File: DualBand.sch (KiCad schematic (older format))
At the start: 23 parts, among them U1 LM7322QMAX/NOPB

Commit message: Connecting MCU
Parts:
- added C? (x2): 1u, symbol C
- added C? (x2): 0.01u, symbol C
- added R? (x2): R, symbol R
- added R?: 12k, symbol R
- added R?: 78.7k, symbol R
- added U?: LMH6703MA/NOPB, symbol LMH6703MA/NOPB
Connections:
- net labels added: DataIn
- wire segments 61 -> 96
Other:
- moved on the sheet: C?, D?, P?, R?, U1, U?

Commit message: Schematic almost finished. Needs headers and test points.
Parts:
- added C1, C10, C12, C2, C6, C8: 1u, symbol C
- added C11, C14, C3, C4, C5, C7, C9: 0.01u, symbol C
- added J1: Conn_01x02_Male, symbol Conn_01x02_Male
- added J2: Conn_01x16_Male, symbol Conn_01x16_Male
- added J3: Conn_01x01_Male, symbol Conn_01x01_Male
- added P1: CONN_01X03, symbol CONN_01X03
- added R3, R4: 10k, symbol R
- added SW1: SW_Push, symbol SW_Push
- R10, R13: renamed from R?; value R -> 100
- R11: renamed from R?; value 287 -> 75
- R14: renamed from R?; value R -> 220
- R7: renamed from R?; value R -> 3k
- R8: renamed from R?; value R -> 10
- R9: renamed from R?; value 500 -> 250
- gave numbers to parts that had none: 24
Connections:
- net labels added: +3.3V, -4.5V, DVCC, DataSignalIn, P4.0, PowerSignalIn, ~SD
- net labels removed: DataIn, DataOut, PowerSignal
- wire segments 96 -> 189
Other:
- note added: "Signal Out"
- moved on the sheet: R1, R2

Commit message: Schematic finished. Need to select footprint for 2 more parts
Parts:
- removed C10, C2, C6, C8: 1u, symbol C
- removed C11, C4, C7, C9: 0.01u, symbol C
- removed J2: Conn_01x16_Male, symbol Conn_01x16_Male
- removed P1: CONN_01X03, symbol CONN_01X03
- removed U2: MSP430F5437AIPN, symbol MSP430F5437AIPN
- added J2, J5, J7: Conn_01x03_Male, Pin_Headers:Pin_Header_Straight_1x03_Pitch2.54mm, symbol Conn_01x03_Male
- added J4, J6: Conn_01x10_Male, Pin_Headers:Pin_Header_Straight_1x10_Pitch2.54mm, symbol Conn_01x10_Male
- added U2: MSP430FR2311IPW20R, Housings_SSOP:TSSOP-20_4.4x6.5mm_Pitch0.65mm, symbol MSP430FR2311IPW20R
- C1, C12, C13, C14, C15, C16, C17, C18, C19, C20, C21, C22, C23, C24, C25, C26, C3, C5: footprint (none) -> Capacitors_SMD:C_0603
- J1: footprint (none) -> Pin_Headers:Pin_Header_Straight_1x02_Pitch2.54mm
- J3: footprint (none) -> Pin_Headers:Pin_Header_Straight_1x01_Pitch2.54mm
- P2: footprint (none) -> Housings_SSOP:TSSOP-14_4.4x5mm_Pitch0.65mm
- R1, R10, R11, R12, R13, R14, R15, R2, R3, R4, R5, R6, R7, R8, R9: footprint (none) -> Resistors_SMD:R_0603
- U3, U4: footprint (none) -> Housings_SOIC:SOIC-8_3.9x4.9mm_Pitch1.27mm
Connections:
- net labels added: DataOut
- net labels removed: P4.0
- wire segments 189 -> 182
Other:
- note removed: "Signal Out"
- moved on the sheet: C1, C3, C5, J1, J3, R1, R2, R3, R4, SW1

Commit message: Selected footprints
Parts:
- D1: footprint (none) -> MyLib:D_0201
- SW1: footprint (none) -> MyLib:FSM2JSMAATR
- U3, U4: symbol LMH6703MA/NOPB -> LMH6703MA/NOPB-RESCUE-DualBand
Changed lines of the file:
@@
 EESchema Schematic File Version 2
+LIBS:DualBand-rescue
 LIBS:power
 LIBS:device
@@
 NoConn ~ 7400 4450
 $Comp
-L LMH6703MA/NOPB U3
+L LMH6703MA/NOPB-RESCUE-DualBand U3
 U 1 1 59EA55FF
 P 8400 3800
@@
 F 0 "D1" H 10400 3850 50  0000 C CNN
 F 1 "SMS7630-061" H 10400 3650 50  0000 C CNN
-F 2 "" H 10400 3750 50  0001 C CNN
+F 2 "MyLib:D_0201" H 10400 3750 50  0001 C CNN
 F 3 "" H 10400 3750 50  0001 C CNN
 	1    10400 3750
@@
 $EndComp
 $Comp
-L LMH6703MA/NOPB U4
+L LMH6703MA/NOPB-RESCUE-DualBand U4
 U 1 1 59EDBD2C
 P 9600 3750
@@
 F 0 "SW1" H 1500 2050 50  0000 L CNN
 F 1 "SW_Push" H 1450 1890 50  0000 C CNN
-F 2 "" H 1450 2150 50  0001 C CNN
+F 2 "MyLib:FSM2JSMAATR" H 1450 2150 50  0001 C CNN
 F 3 "" H 1450 2150 50  0001 C CNN
 	1    1450 1950

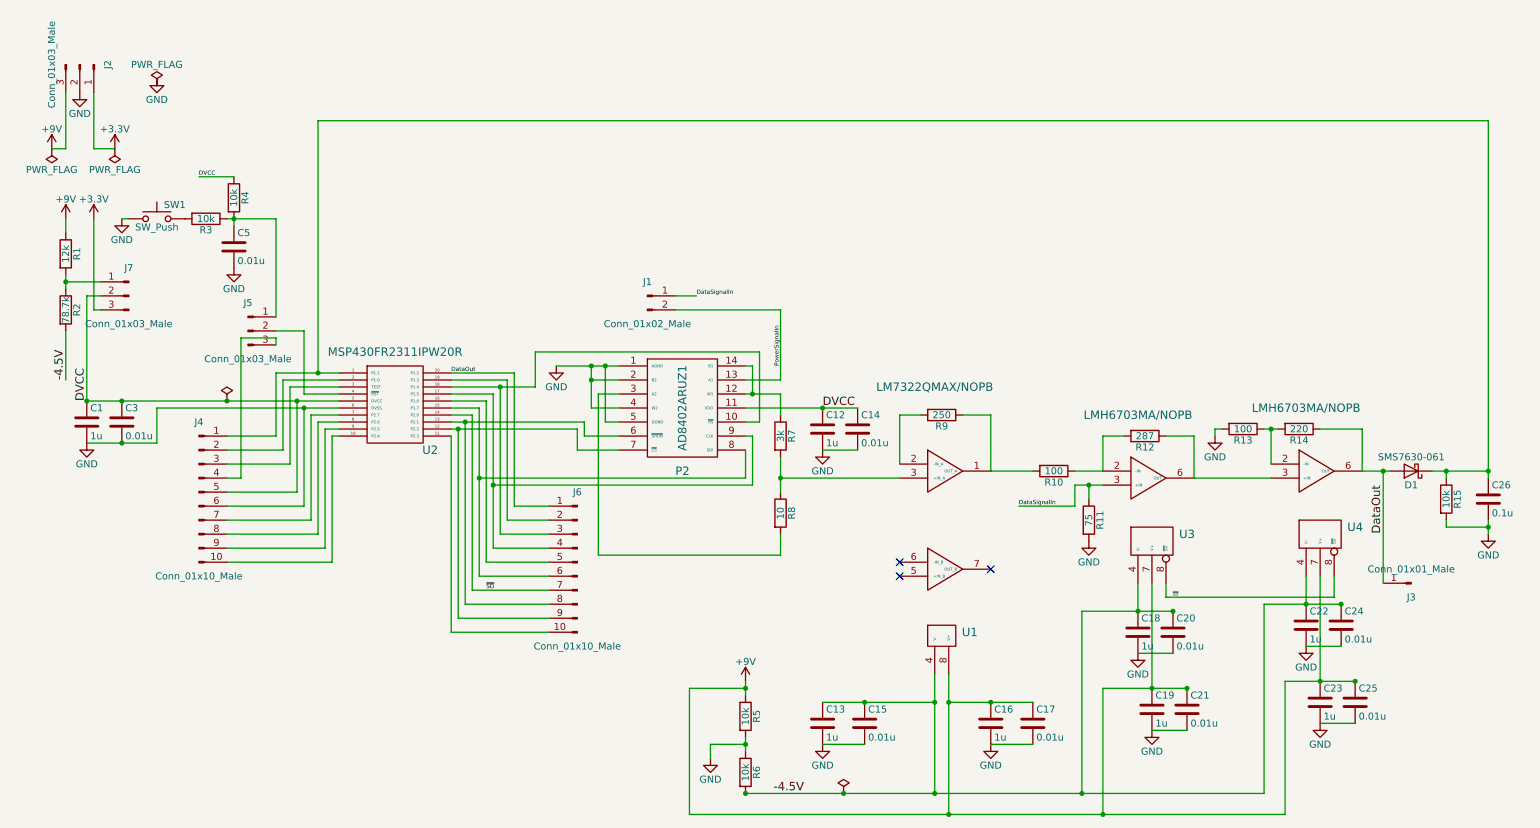
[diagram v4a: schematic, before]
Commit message: Fixed DC levels of amplifiers. Added 3.3V regulator
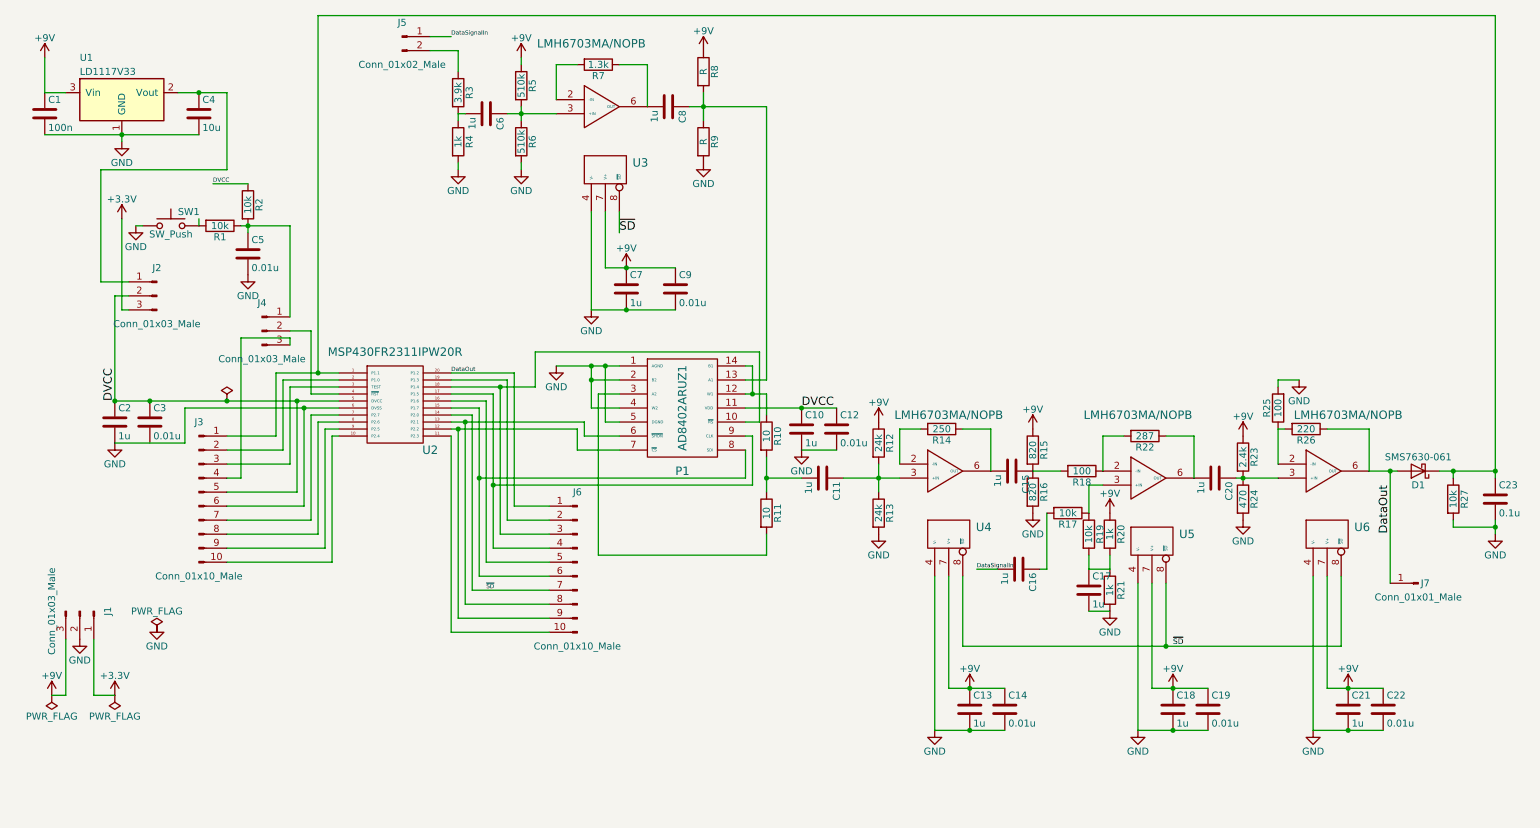
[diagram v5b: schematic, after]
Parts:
- removed C13, C19, C23: 1u, Capacitors_SMD:C_0603, symbol C
- removed C24, C25: 0.01u, Capacitors_SMD:C_0603, symbol C
- removed R1: 12k, Resistors_SMD:R_0603, symbol R
- removed R11: 75, Resistors_SMD:R_0603, symbol R
- removed R2: 78.7k, Resistors_SMD:R_0603, symbol R
- removed U1: LM7322QMAX/NOPB, Housings_SOIC:SOIC-8_3.9x4.9mm_Pitch1.27mm, symbol LM7322QMAX/NOPB
- added C1: 100n, Capacitors_SMD:C_0603, symbol C
- added C11, C16, C17, C20, C6, C7, C8: 1u, Capacitors_SMD:C_0603, symbol C
- added C4: 10u, Capacitors_SMD:C_0603, symbol C
- added C9: 0.01u, Capacitors_SMD:C_0603, symbol C
- added R12, R13: 24k, Resistors_SMD:R_0603, symbol R
- added R15, R16: 820, Resistors_SMD:R_0603, symbol R
- added R17, R19: 10k, Resistors_SMD:R_0603, symbol R
- added R20, R21, R4: 1k, Resistors_SMD:R_0603, symbol R
- added R23: 2.4k, Resistors_SMD:R_0603, symbol R
- added R24: 470, Resistors_SMD:R_0603, symbol R
- added R3: 3.9k, Resistors_SMD:R_0603, symbol R
- added R7: 1.3k, Resistors_SMD:R_0603, symbol R
- added R8, R9: R, Resistors_SMD:R_0603, symbol R
- added U1: LD1117V33, TO_SOT_Packages_THT:TO-220-3_Vertical, symbol LD1117V33
- added U3, U4: LMH6703MA/NOPB, Housings_SOIC:SOIC-8_3.9x4.9mm_Pitch1.27mm, symbol LMH6703MA/NOPB
- C15, C21: value 0.01u -> 1u
- C22: value 1u -> 0.01u
- R10: renamed from R7; value 3k -> 10
- R5, R6: value 10k -> 510k
- renumbered C12 to C10, C14 to C12, C16 to C13, C17 to C14, C20 to C19, C1 to C2, C26 to C23, J2 to J1, J7 to J2, J4 to J3, J5 to J4, J1 to J5, J3 to J7, P2 to P1, R3 to R1, R8 to R11, R9 to R14, R10 to R18, R4 to R2, R12 to R22, R13 to R25, R14 to R26, R15 to R27, U3 to U5, U4 to U6
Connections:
- net +9V: now also C18.1, C19.1, C22.1, C1.1, C7.1, C9.1, R12.1, R15.1, R20.1, R23.1, R8.1, U1.3 (Vin), U3.7 (V+), U4.7 (V+)
- net DataSignalIn: now also C16.2; no longer U5.3 (+IN)
- net GND: now also R6.2, U5.4 (V-), U6.4 (V-), C1.2, C17.2, C4.2, C7.2, C9.2, R13.2, R16.2, R21.2, R24.2, R4.2, R9.2, U1.1 (GND), U3.4 (V-), U4.4 (V-); no longer C15.2, C3.2, R5.2, R6.1
- net ~SD: now also U3.8 (~SD), U4.8 (~SD)
- net at R14.1: now also C15.2, U4.6 (OUT); no longer R18.2
- net at R14.2: now also U4.2 (-IN)
- net at R10.2, R11.1: now also C11.2
- net at R22.1, U5.6 (OUT): now also C20.2; no longer U6.3 (+IN)
- net at J2.1 (Pin_1): now also C4.1, U1.2 (Vout)
- removed net -4.5V: C15.1, C18.1, C19.1, C22.1, R6.2, U5.4 (V-), U6.4 (V-)
- net PowerSignalIn: no longer names the net of P1.13 (A1)
- net PowerSignalIn: now also C8.1, R8.2, R9.1; no longer J5.2 (Pin_2)
- new net: R17.1, R19.1, U5.3 (+IN)
- new net: C15.1, R15.2, R16.1, R18.2
- new net: C20.1, R23.2, R24.1, U6.3 (+IN)
- new net: J5.2 (Pin_2), R3.1
- new net: C6.2, R3.2, R4.1
- new net: C11.1, R12.2, R13.1, U4.3 (+IN)
- new net: C6.1, R5.2, R6.1, U3.3 (+IN)
- new net: C8.2, R7.1, U3.6 (OUT)
- new net: R7.2, U3.2 (-IN)
- new net: C16.1, R17.2
- new net: C17.1, R19.2, R20.2, R21.1
- no-connect marks 3 -> 0
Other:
- moved on the sheet: C10, C12, C13, C14, C18, C19, C2, C23, C3, C5, D1, J1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

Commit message: Revised PCB
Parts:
- added C24: 1u, Capacitors_SMD:C_0603, symbol C
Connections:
- net DataOut: now also C24.1; no longer R26.1, U6.6 (OUT)
- net GND: now also C3.2
- new net: C24.2, R26.1, U6.6 (OUT)
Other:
- moved on the sheet: D1, J7
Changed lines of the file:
@@
 LIBS:bosch
 LIBS:brooktre
-LIBS:Connector
 LIBS:dc-dc
 LIBS:Diode
 LIBS:Display
-LIBS:driver_gate
-LIBS:DSP_Microchip_DSPIC33
 LIBS:elec-unifil
 LIBS:ESD_Protection
-LIBS:Espressif
-LIBS:FPGA_Actel
 LIBS:ftdi
 LIBS:gennum
-LIBS:Graphic
 LIBS:hc11
 LIBS:infineon
@@
 LIBS:ir
 LIBS:Lattice
-LIBS:LED
 LIBS:LEM
-LIBS:Logic_74xgxx
-LIBS:Logic_74xx
-LIBS:Logic_CMOS_4000
-LIBS:Logic_CMOS_IEEE
 LIBS:logic_programmable
-LIBS:Logic_TTL_IEEE
 LIBS:maxim
-LIBS:MCU_Microchip_PIC10
-LIBS:MCU_Microchip_PIC12
-LIBS:MCU_Microchip_PIC16
-LIBS:MCU_Microchip_PIC18
-LIBS:MCU_Microchip_PIC24
-LIBS:MCU_Microchip_PIC32
-LIBS:MCU_NXP_Kinetis
-LIBS:MCU_NXP_LPC
-LIBS:MCU_NXP_S08
-LIBS:MCU_ST_STM8
-LIBS:MCU_ST_STM32
-LIBS:MCU_Texas_MSP430
 LIBS:Mechanical
 LIBS:modules
-LIBS:Motor
 LIBS:motor_drivers
 LIBS:nordicsemi
@@
 LIBS:pspice
 LIBS:references
-LIBS:Relay
 LIBS:rfcom
 LIBS:RFSolutions
-LIBS:Sensor_Current
 LIBS:sensors
 LIBS:silabs
 LIBS:supertex
-LIBS:Switch
-LIBS:Transformer
-LIBS:Transistor
 LIBS:triac_thyristor
-LIBS:Valve
 LIBS:video
 LIBS:wiznet
@@
 L D_Schottky D1
 U 1 1 59EB786E
-P 10450 3750
-F 0 "D1" H 10450 3850 50  0000 C CNN
-F 1 "SMS7630-061" H 10450 3650 50  0000 C CNN
-F 2 "MyLib:D_0201" H 10450 3750 50  0001 C CNN
-F 3 "" H 10450 3750 50  0001 C CNN
-	1    10450 3750
+P 10550 3750
+F 0 "D1" H 10550 3850 50  0000 C CNN
+F 1 "SMS7630-061" H 10400 3650 50  0000 C CNN
+F 2 "MyLib:D_0201" H 10550 3750 50  0001 C CNN
+F 3 "" H 10550 3750 50  0001 C CNN
+	1    10550 3750
 	-1   0    0    1
 $EndComp
@@
 L Conn_01x01_Male J7
 U 1 1 59F2BCE3
-P 10450 4550
-F 0 "J7" H 10400 4550 50  0000 C CNN
-F 1 "Conn_01x01_Male" H 10450 4650 50  0000 C CNN
-F 2 "Pin_Headers:Pin_Header_Straight_1x01_Pitch2.54mm" H 10450 4550 50  0001 C CNN
-F 3 "" H 10450 4550 50  0001 C CNN
-	1    10450 4550
+P 10600 4500
+F 0 "J7" H 10550 4500 50  0000 C CNN
+F 1 "Conn_01x01_Male" H 10600 4600 50  0000 C CNN
+F 2 "Pin_Headers:Pin_Header_Straight_1x01_Pitch2.54mm" H 10600 4500 50  0001 C CNN
+F 3 "" H 10600 4500 50  0001 C CNN
+	1    10600 4500
 	-1   0    0    1
 $EndComp
@@
 	1    0    0    -1
 $EndComp
-Text Label 10250 3850 3    60   ~ 0
+Text Label 10400 4050 3    60   ~ 0
 DataOut
 Text Label 3550 3050 0    30   ~ 0
@@
 	1150 3250 2750 3250
 Wire Wire Line
-	1150 3550 1650 3550
-Wire Wire Line
 	1200 2600 1200 1950
 Wire Wire Line
@@
 	7300 4450 7450 4450
 Wire Wire Line
-	10600 3750 11000 3750
-Wire Wire Line
-	10100 3750 10300 3750
+	10700 3750 11000 3750
 Wire Wire Line
 	10100 3450 10100 3750
@@
 	1150 2500 1250 2500
 Wire Wire Line
-	10250 3750 10250 4550
-Connection ~ 10250 3750
+	10400 3750 10400 4500
 Wire Wire Line
 	1300 2000 1350 2000
@@
 $EndComp
 Connection ~ 9200 3800
+$Comp
+L C C24
+U 1 1 5A1DC42E
+P 10250 3750
+F 0 "C24" H 10275 3850 50  0001 L CNN
+F 1 "1u" H 10275 3650 50  0000 L CNN
+F 2 "Capacitors_SMD:C_0603" H 10288 3600 50  0001 C CNN
+F 3 "" H 10250 3750 50  0001 C CNN
+	1    10250 3750
+	0    1    1    0
+$EndComp
+Wire Wire Line
+	1150 3550 1650 3550
+Connection ~ 1400 3550
 $EndSCHEMATC
